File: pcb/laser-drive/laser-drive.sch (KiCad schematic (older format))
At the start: 19 parts, among them P1 5V-in, P2 Laser, P3 DATA, P6 12V-in, Q1 BC309, Q2 BCP5616Q, Q3 MTM232270

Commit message: o laser driver: change to use OpAmp.
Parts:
- removed C1, C4: 100n, Capacitors_SMD:C_0805, symbol C
- removed C2, C3, C5: 10u, Capacitors_SMD:C_1206_HandSoldering, symbol C
- removed P1: 5V-in, Pin_Headers:Pin_Header_Straight_1x02, symbol CONN_01X02
- removed P2: Laser, Pin_Headers:Pin_Header_Straight_1x02, symbol CONN_01X02
- removed P3: DATA, Pin_Headers:Pin_Header_Straight_1x02, symbol CONN_01X02
- removed P6: 12V-in, Pin_Headers:Pin_Header_Straight_1x02, symbol CONN_01X02
- removed Q1: BC309, TO_SOT_Packages_THT:TO-92_Horizontal1_Molded_Narrow, symbol Q_PNP_CBE
- removed Q2: BCP5616Q, TO_SOT_Packages_SMD:SOT-223, symbol Q_NPN_BCE
- removed Q3: MTM232270, TO_SOT_Packages_SMD:SOT-323, symbol Q_NMOS_GSD
- removed R1: 100k, Capacitors_SMD:C_0603, symbol R
- removed R2, R3: R, Capacitors_SMD:C_0603, symbol R
- removed R4: 100, Resistors_SMD:R_0603, symbol R
- removed R5: 4R7, Resistors_ThroughHole:Resistor_Horizontal_RM15mm, symbol R
- removed R6: 470, Resistors_SMD:R_0603, symbol R
- removed RV1: POT, Potentiometers:Potentiometer_WirePads_Small, symbol POT
- added C6, C7, C9: 100n, Capacitors_SMD:C_0805, symbol C
- added C8, C? (x6): 10u, Capacitors_SMD:C_1210, symbol C
- added P4: Laser, Pin_Headers:Pin_Header_Straight_1x02, symbol CONN_01X02
- added P5: 12V-in, Pin_Headers:Pin_Header_Straight_1x02, symbol CONN_01X02
- added P7: DATA, Pin_Headers:Pin_Header_Straight_1x02, symbol CONN_01X02
- added Q4: BCP5616Q, TO_SOT_Packages_SMD:SOT-223, symbol Q_NPN_BCE
- added Q5: MTM232270, TO_SOT_Packages_SMD:SOT-323, symbol Q_NMOS_GSD
- added R10, R11: 470, Resistors_SMD:R_0603, symbol R
- added R12: 100k, Capacitors_SMD:C_0603, symbol R
- added R7, R8: R, Capacitors_SMD:C_0603, symbol R
- added R9: 4R7, Resistors_ThroughHole:Resistor_Horizontal_RM15mm, symbol R
- added RV2: POT, Potentiometers:Potentiometer_WirePads, symbol POT
- added U1: MIC920, TO_SOT_Packages_SMD:SC-70-5, symbol MIC920
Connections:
- net labels added: +12VA, GNDA, LaserOut2
- net labels removed: +12V, +5V, GND, LaserOut
- wire segments 35 -> 36
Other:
- note removed: "<- Thermally\n couple ->"
- note removed: "≈1.9V"

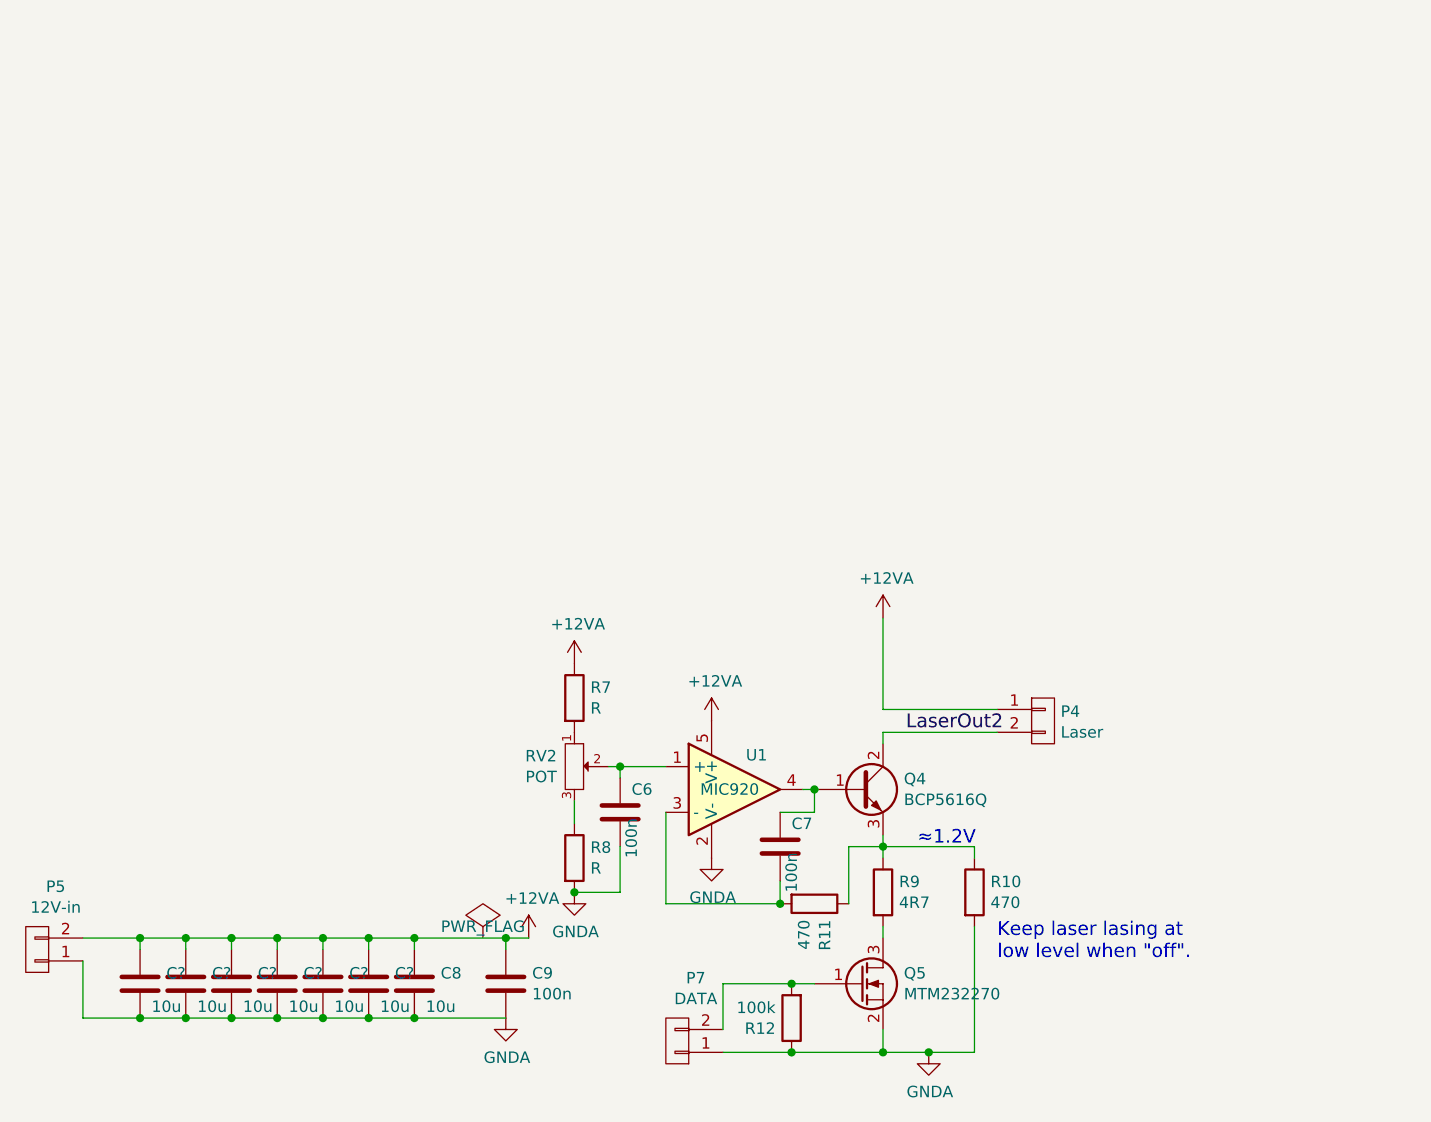
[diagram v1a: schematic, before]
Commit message: o Update cape: include hsync circuit o Laser driver: new board that uses the new OpAmp circuit   (not tested yet)
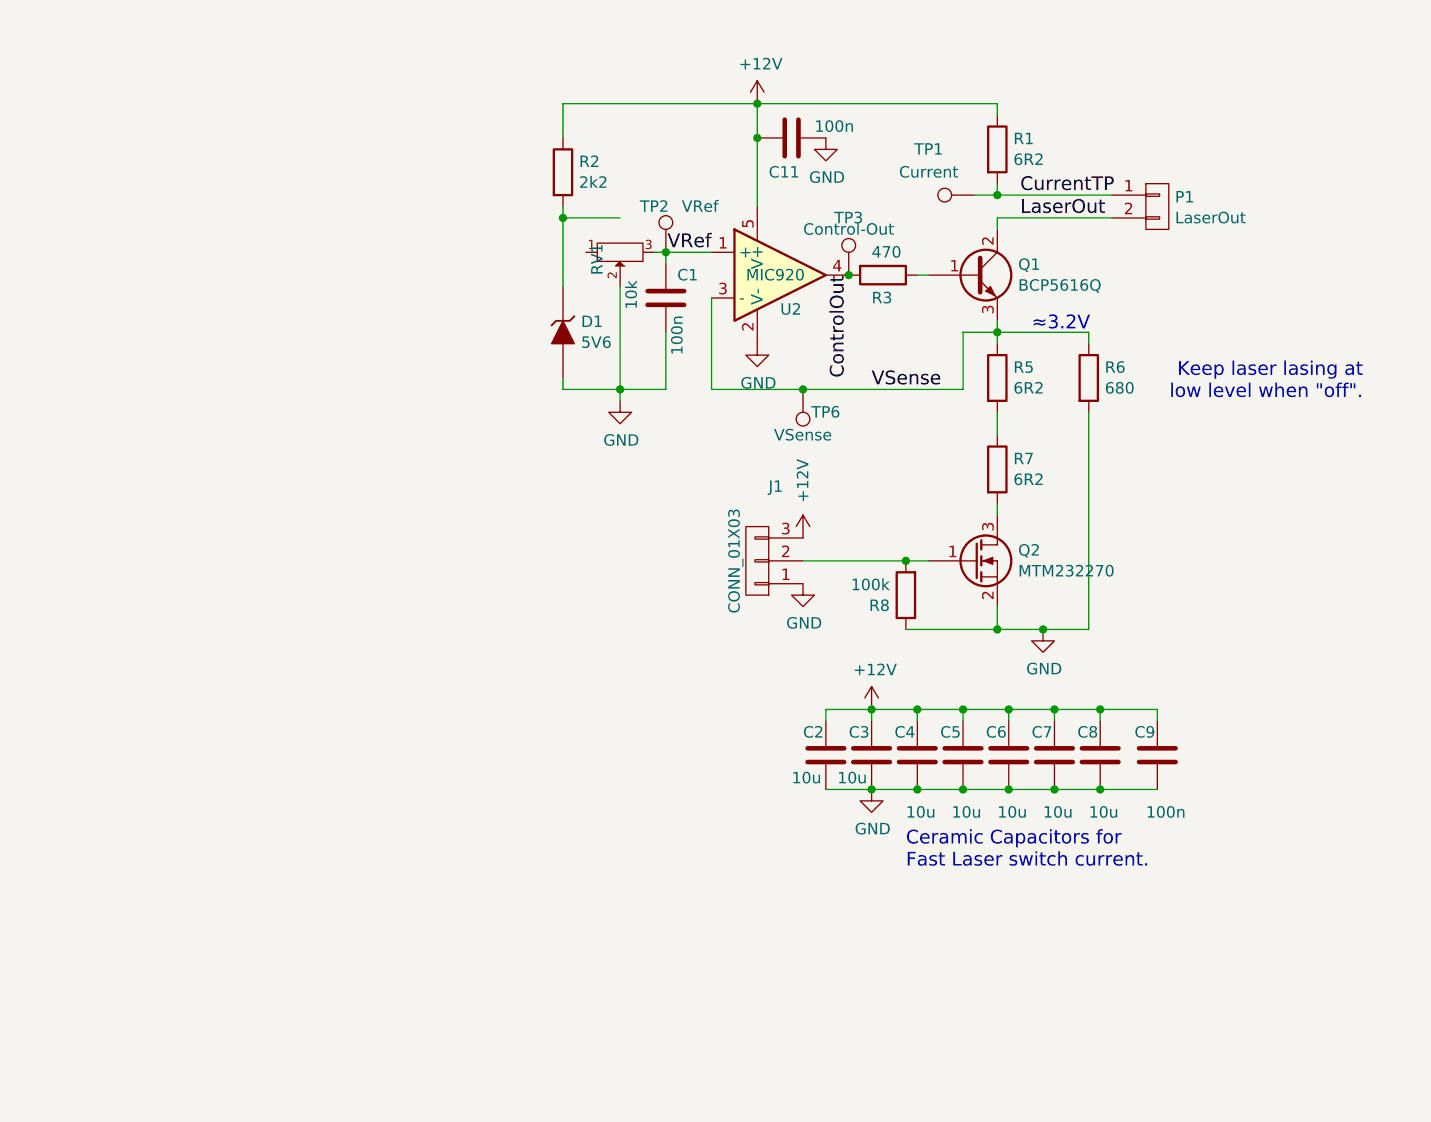
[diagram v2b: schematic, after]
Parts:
- removed C? (x6): 10u, Capacitors_SMD:C_1210, symbol C
- removed P4: Laser, Pin_Headers:Pin_Header_Straight_1x02, symbol CONN_01X02
- removed P5: 12V-in, Pin_Headers:Pin_Header_Straight_1x02, symbol CONN_01X02
- removed P7: DATA, Pin_Headers:Pin_Header_Straight_1x02, symbol CONN_01X02
- removed Q4: BCP5616Q, TO_SOT_Packages_SMD:SOT-223, symbol Q_NPN_BCE
- removed Q5: MTM232270, TO_SOT_Packages_SMD:SOT-323, symbol Q_NMOS_GSD
- removed R10, R11: 470, Resistors_SMD:R_0603, symbol R
- removed R12: 100k, Capacitors_SMD:C_0603, symbol R
- removed R9: 4R7, Resistors_ThroughHole:Resistor_Horizontal_RM15mm, symbol R
- removed RV2: POT, Potentiometers:Potentiometer_WirePads, symbol POT
- removed U1: MIC920, TO_SOT_Packages_SMD:SC-70-5, symbol MIC920
- added C1, C11: 100n, Capacitors_SMD:C_0603, symbol C
- added C2, C3, C4, C5: 10u, Capacitors_SMD:C_1210, symbol C
- added D1: 5V6, Diodes_SMD:D_SOD-323_HandSoldering, symbol ZENER
- added J1: CONN_01X03, Pin_Headers:Pin_Header_Straight_1x03_Pitch2.54mm, symbol CONN_01X03
- added P1: LaserOut, Pin_Headers:Pin_Header_Straight_1x02, symbol CONN_01X02
- added Q1: BCP5616Q, TO_SOT_Packages_SMD:SOT-223, symbol Q_NPN_BCE
- added Q2: MTM232270, TO_SOT_Packages_SMD:SOT-323_SC-70, symbol Q_NMOS_GSD
- added R1, R5: 6R2, Resistors_SMD:R_2512, symbol R
- added R2: 2k2, Resistors_SMD:R_0603, symbol R
- added R3: 470, Resistors_SMD:R_0603, symbol R
- added R6: 680, Resistors_SMD:R_0603, symbol R
- added RV1: 10k, Potentiometers:Potentiometer_WirePads, symbol POT
- added TP1: Current, Measurement_Points:Measurement_Point_Round-SMD-Pad_Small, symbol TEST_1P
- added TP2: VRef, Measurement_Points:Measurement_Point_Round-SMD-Pad_Small, symbol TEST_1P
- added TP3: Control-Out, Measurement_Points:Measurement_Point_Round-SMD-Pad_Small, symbol TEST_1P
- added TP6: VSense, Measurement_Points:Measurement_Point_Round-SMD-Pad_Small, symbol TEST_1P
- added U2: MIC920, TO_SOT_Packages_SMD:SOT-353_SC-70-5, symbol MIC920
- C6, C7: value 100n -> 10u; footprint Capacitors_SMD:C_0805 -> Capacitors_SMD:C_1210
- R7: value R -> 6R2; footprint Capacitors_SMD:C_0603 -> Resistors_SMD:R_2512; Power (none) -> 1W
- R8: value R -> 100k
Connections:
- net +12V: now reaches C6.1
- net +12V: now also C7.1, C8.1, C9.1, C11.2, C2.1, C3.1, C4.1, C5.1, J1.3 (P3), R1.1, R2.1, U2.5 (V+)
- net GND: now reaches C7.2
- net GND: now also C6.2, C8.2, C9.2, R8.1, C1.2, C11.1, C2.2, C3.2, C4.2, C5.2, D1.2 (A), J1.1 (P1), Q2.2 (S), R6.2, RV1.2, U2.2 (V-)
- net at R7.2: now also Q2.3 (D)
- removed net +12VA: C8.1, C9.1, R7.1
- removed net GNDA: C6.2, C8.2, C9.2, R8.2
- new net: R5.2, R7.1
- new net: J1.2 (P2), Q2.1 (G), R8.2
- new net: Q1.1 (B), R3.1
- new net: D1.1 (K), R2.2
- new net ControlOut: R3.2, TP3.1, U2.4
- new net CurrentTP: P1.1 (P1), R1.2, TP1.1
- new net LaserOut: P1.2 (P2), Q1.2 (C)
- new net VRef: C1.1, RV1.3, TP2.1, U2.1 (+)
- new net VSense: Q1.3 (E), R5.1, R6.1, TP6.1, U2.3 (-)
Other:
- note added: "Ceramic Capacitors for\nFast Laser switch current."
- note added: "≈3.2V"
- note removed: "≈1.2V"

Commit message: o Add pictures for laser driver.
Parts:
- RV1: symbol POT -> POT-RESCUE-laser-drive
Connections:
- net GND: now also RV1.1; no longer RV1.2
- net VRef: now also RV1.2; no longer RV1.3
- net at D1.1 (K), R2.2: now also RV1.3
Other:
- moved on the sheet: RV1
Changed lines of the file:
@@
 EESchema Schematic File Version 2
+LIBS:laser-drive-rescue
 LIBS:power
 LIBS:device
@@
 $EndComp
 $Comp
-L POT RV1
+L POT-RESCUE-laser-drive RV1
 U 1 1 58D4177B
 P 4450 1900
-F 0 "RV1" V 4350 2000 50  0000 R CNN
-F 1 "10k" V 4500 2150 50  0000 R CNN
+F 0 "RV1" V 4400 1800 50  0000 R CNN
+F 1 "10k" H 4500 1900 50  0000 R CNN
 F 2 "Potentiometers:Potentiometer_WirePads" H 4450 1900 50  0001 C CNN
 F 3 "" H 4450 1900 50  0000 C CNN
 	1    4450 1900
-	1    0    0    1
+	0    1    -1   0
 $EndComp
 $Comp

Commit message: o Change footprint trimmer to actual size.
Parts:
- RV1: footprint Potentiometers:Potentiometer_WirePads -> Potentiometers:Potentiometer_WirePads_Small
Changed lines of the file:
@@
 EESchema Schematic File Version 2
-LIBS:laser-drive-rescue
 LIBS:power
-LIBS:device
-LIBS:transistors
-LIBS:conn
-LIBS:linear
-LIBS:regul
-LIBS:74xx
-LIBS:cmos4000
-LIBS:adc-dac
-LIBS:memory
-LIBS:xilinx
-LIBS:microcontrollers
-LIBS:dsp
-LIBS:microchip
-LIBS:analog_switches
-LIBS:motorola
-LIBS:texas
-LIBS:intel
-LIBS:audio
-LIBS:interface
-LIBS:digital-audio
-LIBS:philips
-LIBS:display
-LIBS:cypress
-LIBS:siliconi
-LIBS:opto
-LIBS:atmel
-LIBS:contrib
-LIBS:valves
-LIBS:ldgraphy
 LIBS:laser-drive-cache
 EELAYER 26 0
@@
 F 0 "RV1" V 4400 1800 50  0000 R CNN
 F 1 "10k" H 4500 1900 50  0000 R CNN
-F 2 "Potentiometers:Potentiometer_WirePads" H 4450 1900 50  0001 C CNN
+F 2 "Potentiometers:Potentiometer_WirePads_Small" H 4450 1900 50  0001 C CNN
 F 3 "" H 4450 1900 50  0000 C CNN
 	1    4450 1900

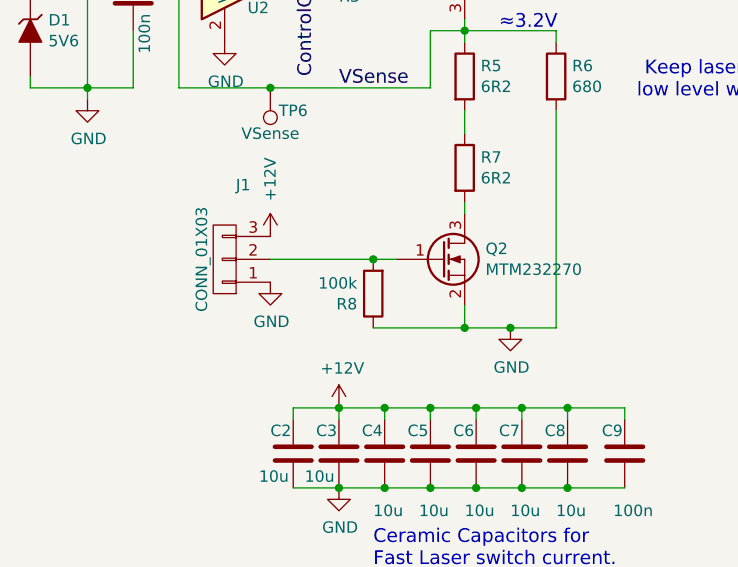
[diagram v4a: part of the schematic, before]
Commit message: o Update footprint resistor.
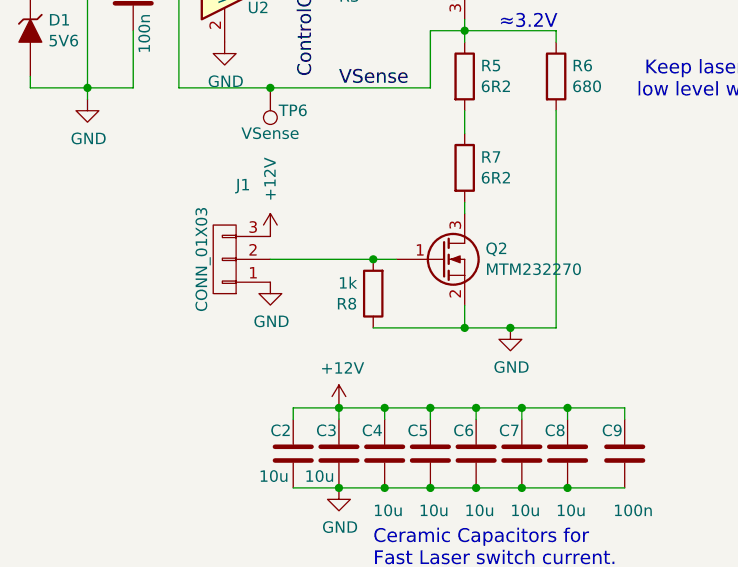
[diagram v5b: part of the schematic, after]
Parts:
- R8: value 100k -> 1k; footprint Capacitors_SMD:C_0603 -> Resistors_SMD:R_0603
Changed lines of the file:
@@
 P 5700 3400
 F 0 "R8" H 5770 3446 50  0000 L CNN
-F 1 "100k" H 5770 3355 50  0000 L CNN
-F 2 "Capacitors_SMD:C_0603" V 5630 3400 50  0001 C CNN
+F 1 "1k" H 5770 3355 50  0000 L CNN
+F 2 "Resistors_SMD:R_0603" V 5630 3400 50  0001 C CNN
 F 3 "" H 5700 3400 50  0000 C CNN
 	1    5700 3400

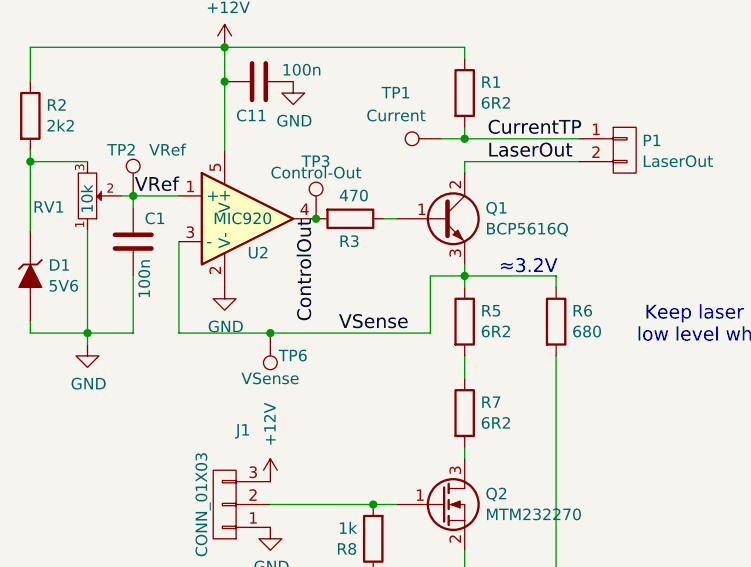
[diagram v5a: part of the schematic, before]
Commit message: Add oscillation suppresion cap for laser driver.
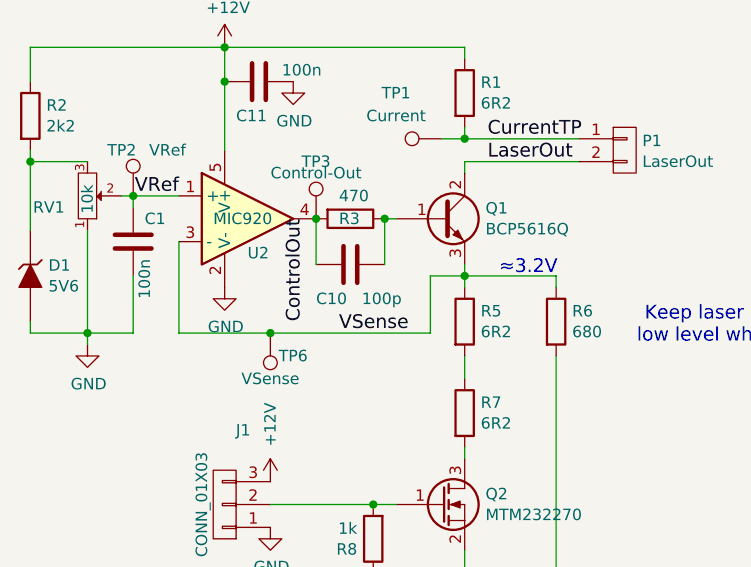
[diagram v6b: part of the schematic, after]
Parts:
- added C10: 100p, Capacitors_SMD:C_0603, symbol C
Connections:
- net ControlOut: no longer R3.2, TP3.1, U2.4
- net at Q1.1 (B), R3.1: now also C10.1
- new net: C10.2, R3.2, TP3.1, U2.4
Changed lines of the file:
@@
 U 1 1 58D4958F
 P 5600 2000
-F 0 "R3" V 5700 1950 50  0000 L CNN
+F 0 "R3" V 5600 1950 50  0000 L CNN
 F 1 "470" V 5500 1950 50  0000 L CNN
 F 2 "Resistors_SMD:R_0603" V 5530 2000 50  0001 C CNN
@@
 Text Label 4850 1900 2    60   ~ 0
 VRef
-Text Label 5450 2000 3    60   ~ 0
+Text Label 5400 2000 3    60   ~ 0
 ControlOut
 $Comp
@@
 	1    0    0    -1
 $EndComp
+$Comp
+L C C10
+U 1 1 59B52DAB
+P 5600 2200
+F 0 "C10" V 5750 2050 50  0000 L CNN
+F 1 "100p" V 5750 2250 50  0000 L CNN
+F 2 "Capacitors_SMD:C_0603" H 5638 2050 50  0001 C CNN
+F 3 "" H 5600 2200 50  0000 C CNN
+	1    5600 2200
+	0    1    1    0
+$EndComp
+Wire Wire Line
+	5450 2000 5450 2200
+Wire Wire Line
+	5750 2200 5750 2000
+Connection ~ 5750 2000
 $EndSCHEMATC
